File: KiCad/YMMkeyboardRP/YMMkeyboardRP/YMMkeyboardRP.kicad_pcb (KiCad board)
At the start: 4 copper layers, 100 x 100 mm, 53 parts, among them J2 Conn_01x02, J3 Conn_02x18_Odd_Even, J4 Conn_02x18_Odd_Even, J6 USB_B_Micro, J7 USB_C_Receptacle_USB2.0_16P, U1 XC6206PxxxMR, U2 W25Q32JVS, U3 RP2040, U5 NCP1117-3.3_SOT223, U7 NCP1117-3.3_SOT223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

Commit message: 主要な配線終わった ピンにどうやって配線するんや
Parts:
- moved C17 83.3 mm to (87.5, 103.7), turned to 90 degrees
- moved R5 82.8 mm to (95.5, 116.0), turned to -90 degrees
- moved C2 80.6 mm to (93.5, 116.2), turned to -90 degrees
- moved C16 80.5 mm to (78.5, 103.7), turned to 90 degrees
- moved C15 80.2 mm to (80.0, 103.7), turned to 90 degrees
- moved C14 79.9 mm to (81.5, 103.7), turned to 90 degrees
- moved C13 79.8 mm to (83.0, 103.7), turned to 90 degrees
- moved C12 79.7 mm to (84.5, 103.7), turned to 90 degrees
- moved C11 77.3 mm to (89.0, 103.7), turned to 90 degrees
- moved R2 77.2 mm to (100.7, 106.0)
- moved C3 76.3 mm to (98.0, 117.0)
- moved Y1 73.5 mm to (94.5, 119.5)
- moved C10 72.1 mm to (100.7, 107.5)
- moved C9 70.0 mm to (86.0, 103.7), turned to 90 degrees
- moved C6 68.7 mm to (92.0, 103.7), turned to 90 degrees
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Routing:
- net /USB_D-: track 27.9 -> 89.2 mm, vias 5 -> 4
- net /USB_D+: track 27.7 -> 86.7 mm
- net /GPIO0: track 0.00 -> 40.5 mm
- net /GPIO1: track 0.00 -> 39.6 mm
- net /GPIO4: track 0.00 -> 38.3 mm
- net /GPIO2: track 0.00 -> 38.2 mm
- net +3V3: track 0.00 -> 31.3 mm
- net /QSPI_SS: track 0.00 -> 13.0 mm, vias 0 -> 2
- net /XIN: track 0.00 -> 8.34 mm
- net +1V1: track 0.00 -> 5.51 mm
- net Net-(C3-Pad1): track 0.00 -> 4.19 mm
- net /~{USB_BOOT}: track 0.00 -> 3.41 mm
- net Net-(U3-USB_DP): track 0.00 -> 2.39 mm
- net Net-(U3-USB_DM): track 0.00 -> 2.32 mm
- net GND: track 0.00 -> 2.28 mm, vias 26 -> 40
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
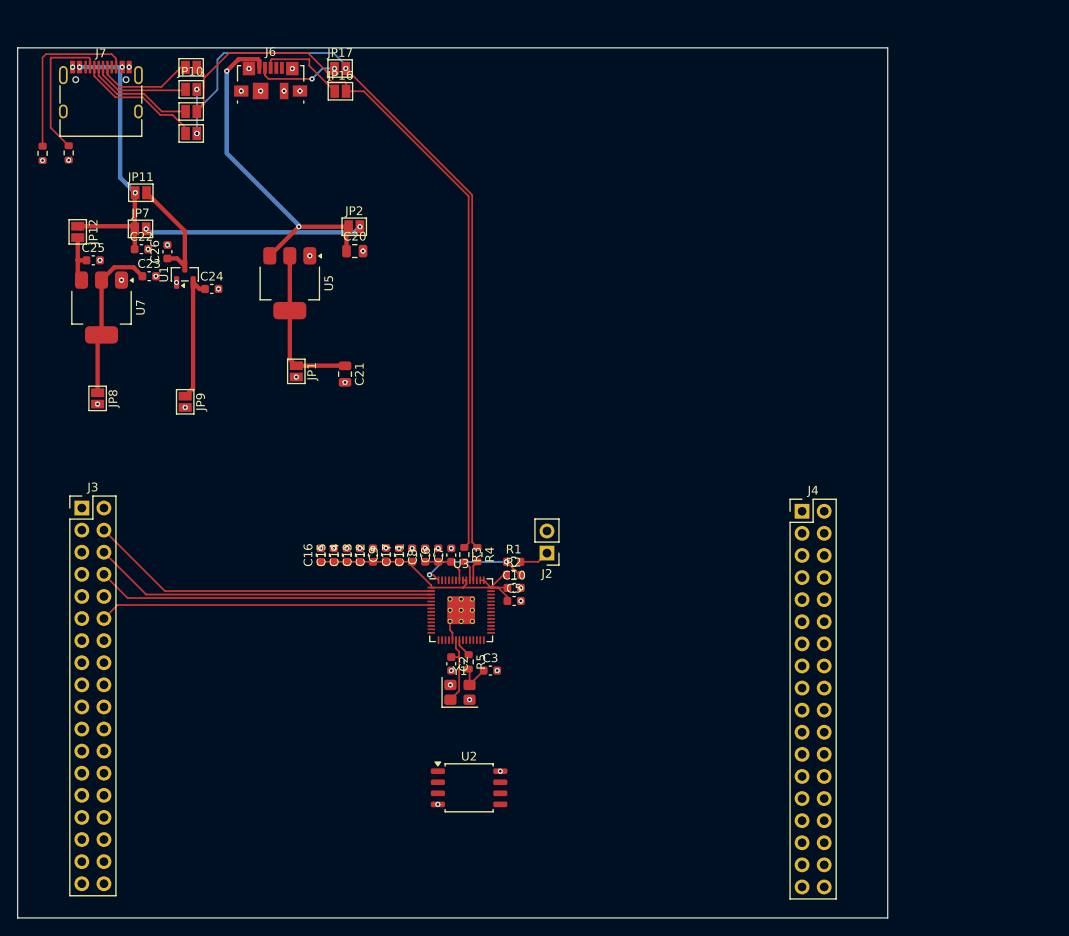
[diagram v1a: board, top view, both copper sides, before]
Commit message: rp2040の独自実装を検討
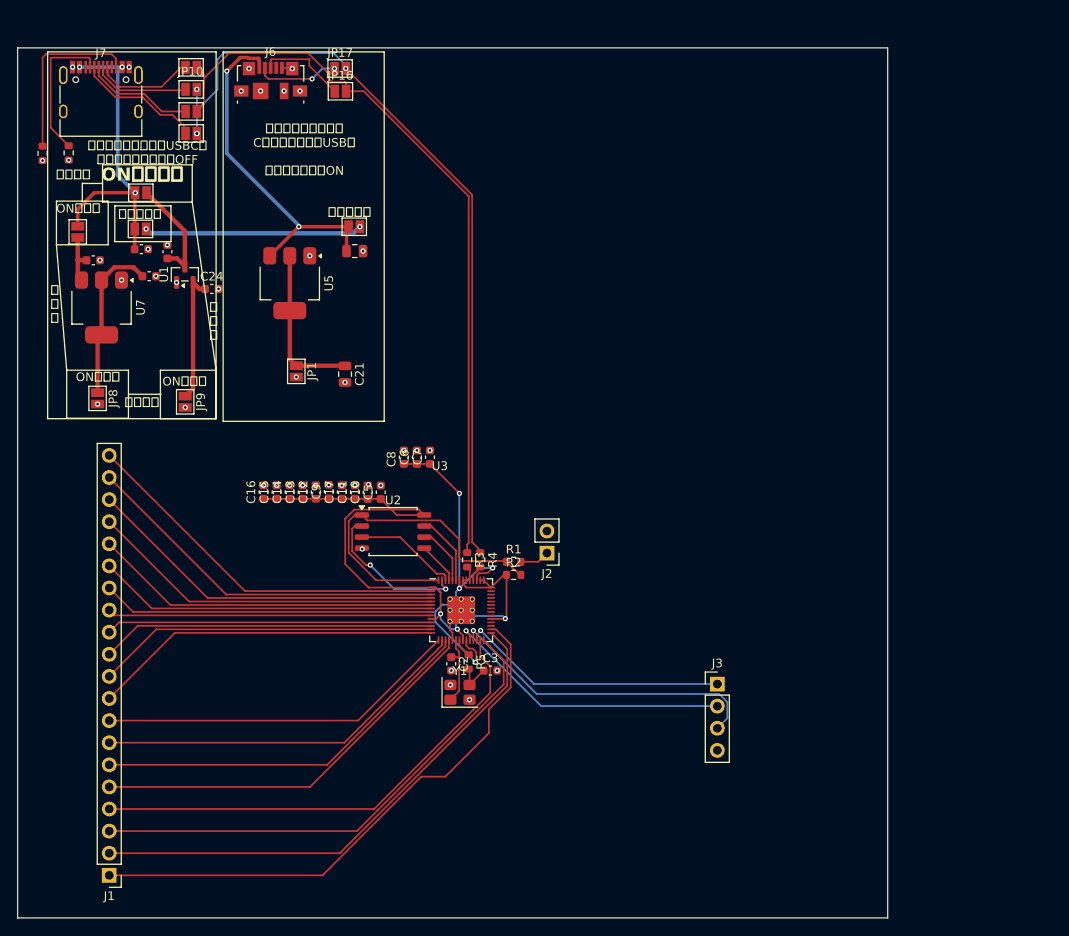
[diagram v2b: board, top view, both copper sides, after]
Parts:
- removed J4: Conn_02x18_Odd_Even, Connector_PinHeader_2.54mm:PinHeader_2x18_P2.54mm_Vertical
- added J1: Conn_01x20_Socket, Connector_PinHeader_2.54mm:PinHeader_1x20_P2.54mm_Vertical, F.Cu at (54.2, 140.5)
- J3: value Conn_02x18_Odd_Even -> Conn_01x04_Socket; footprint Connector_PinHeader_2.54mm:PinHeader_2x18_P2.54mm_Vertical -> Connector_PinHeader_2.54mm:PinHeader_1x04_P2.54mm_Vertical
- moved J3 75.8 mm to (124.1, 118.5)
- moved U2 30.7 mm to (86.8, 101.0)
- moved C10 20.1 mm to (83.9, 96.5), turned to 90 degrees
- moved C5 19.8 mm to (85.4, 96.5), turned to 90 degrees
- moved C6 11.5 mm to (89.5, 92.5)
- moved C7 11.5 mm to (91.0, 92.5)
- moved C8 11.5 mm to (88.0, 92.5)
- moved C11 9.78 mm to (82.4, 96.5)
- moved C12 9.78 mm to (77.9, 96.5)
- moved C13 9.78 mm to (76.4, 96.5)
- moved C14 9.78 mm to (74.9, 96.5)
- moved C15 9.78 mm to (73.4, 96.5)
- moved C16 9.78 mm to (71.9, 96.5)
- moved C17 9.78 mm to (80.9, 96.5)
- moved C9 9.78 mm to (79.4, 96.4)
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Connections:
- J3 pad 1: GND -> /RUN
- J3 pad 2: +3V3 -> /SWCLK
- J3 pad 3: GND -> /SWD
- J3 pad 4: /GPIO0 -> GND
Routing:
- net /GPIO19: track 0.00 -> 64.6 mm
- net /GPIO18: track 0.00 -> 60.6 mm
- net /GPIO17: track 0.00 -> 58.4 mm
- net /GPIO16: track 0.00 -> 55.8 mm
- net +3V3: track 31.3 -> 78.6 mm, vias 4 -> 6
- net /GPIO15: track 0.00 -> 46.6 mm
- net /GPIO14: track 0.00 -> 45.0 mm
- net /GPIO13: track 0.00 -> 43.5 mm
- net /GPIO12: track 0.00 -> 41.7 mm
- net /GPIO3: track 0.00 -> 40.8 mm
- net /GPIO11: track 0.00 -> 40.1 mm
- net /GPIO10: track 0.00 -> 39.2 mm
- net /GPIO5: track 0.00 -> 39.0 mm
- net /GPIO9: track 0.00 -> 38.4 mm
- net /GPIO6: track 0.00 -> 38.2 mm
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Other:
- board text added: "ON 小さい"
- board text added: "ON大きい"
- board text added: "ON小さい"
- board text added: "つながない"
- board text added: "つながないを除いて Cじゃない小さいUSBを 使うならすべてON"
- board text added: "つながないを除いてUSBCを 使わないならすべてOFF"
- board text added: "リ ン ク"
- board text added: "片方のみ"
